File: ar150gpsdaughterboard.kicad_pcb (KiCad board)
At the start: 2 copper layers, 32.2 x 21.2 mm, 7 parts, among them P1 CONN_02X05, Q1 BSS138, U1 QUECTEL-L80

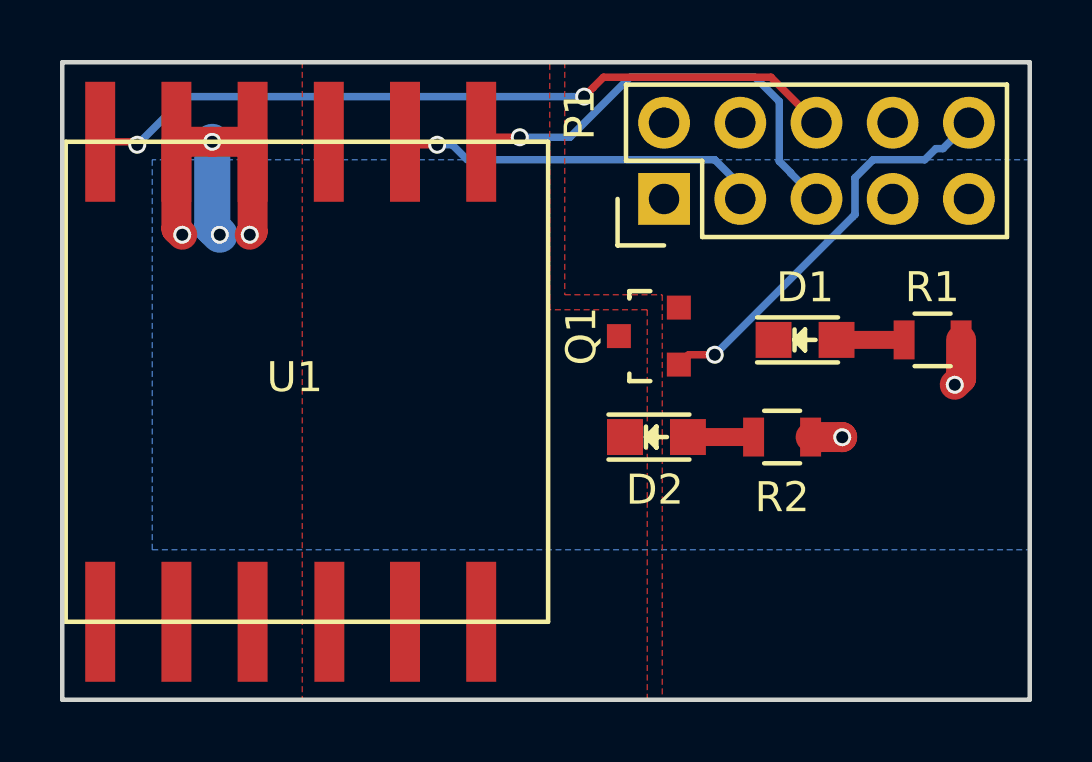
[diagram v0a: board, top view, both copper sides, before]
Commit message: Updated board layout - new L80 footprint, better location of pins
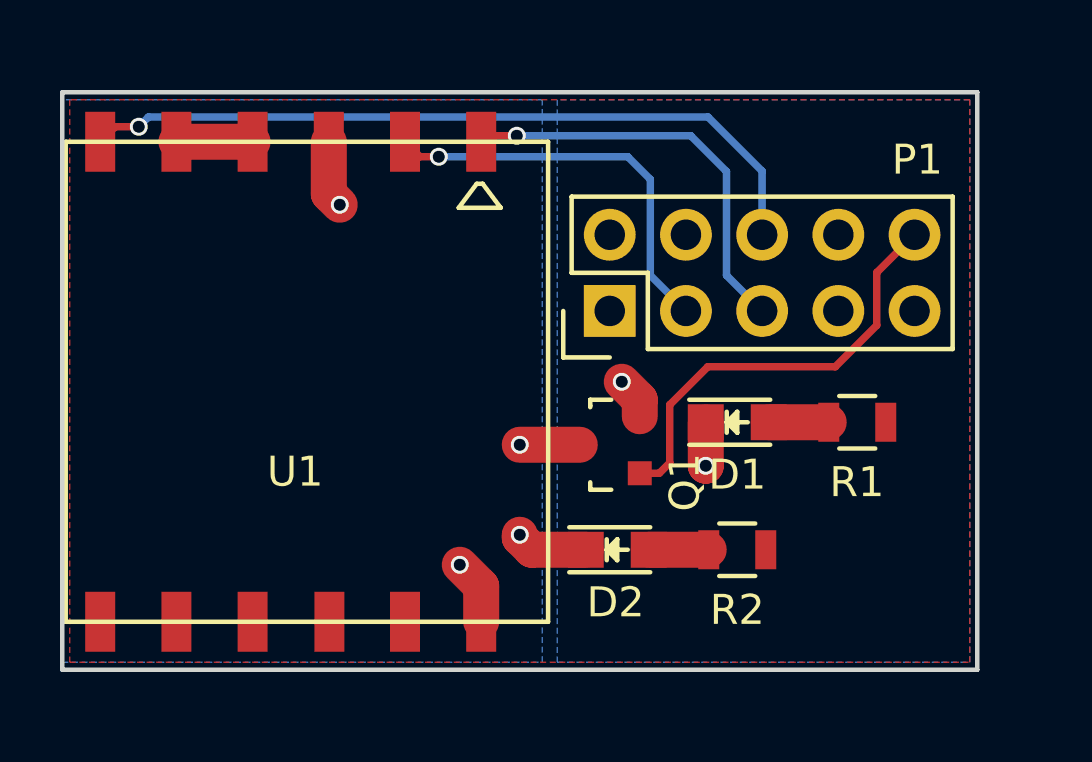
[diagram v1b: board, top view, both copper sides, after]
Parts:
- moved P1 4.15 mm to (137.0, 102.5)
- moved R2 4.04 mm to (141.2, 110.5)
- moved D2 3.98 mm to (137.2, 110.5)
- moved Q1 3.85 mm to (137.0, 107.0)
- moved R1 3.72 mm to (145.2, 106.2)
- moved D1 3.56 mm to (141.2, 106.2)
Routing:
- net +3V3: track 14.7 -> 2.54 mm, vias 6 -> 0
- net GP_GND: track 0.00 -> 8.91 mm, vias 0 -> 4
- net GND: track 0.00 -> 2.85 mm, vias 0 -> 2
- net RX: track 12.2 -> 13.6 mm
- net TX: track 14.9 -> 13.9 mm
- net GP_17: track 13.7 -> 14.6 mm, vias 1 -> 0
- net GP_14: track 25.5 -> 25.3 mm, vias 2 -> 1
- added copper zone on F.Cu, net +3V3
- added copper zone on B.Cu, net GND
- added copper zone on B.Cu, net GP_GND
- removed copper zone on B.Cu, net +3V3
- removed copper zone on F.Cu, net GND
- removed copper zone on F.Cu, net GP_GND
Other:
- board size 32.2 x 21.2 mm -> 30.5 x 19.2 mm
